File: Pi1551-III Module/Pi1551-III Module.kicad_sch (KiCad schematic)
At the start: 21 parts, among them J1 DC IN, J2 C64_IEC, J3 C64_IEC, J8 Module_Panel, M1 Mounting, M2 Mounting, M3 Mounting, M4 Mounting, U1 7406

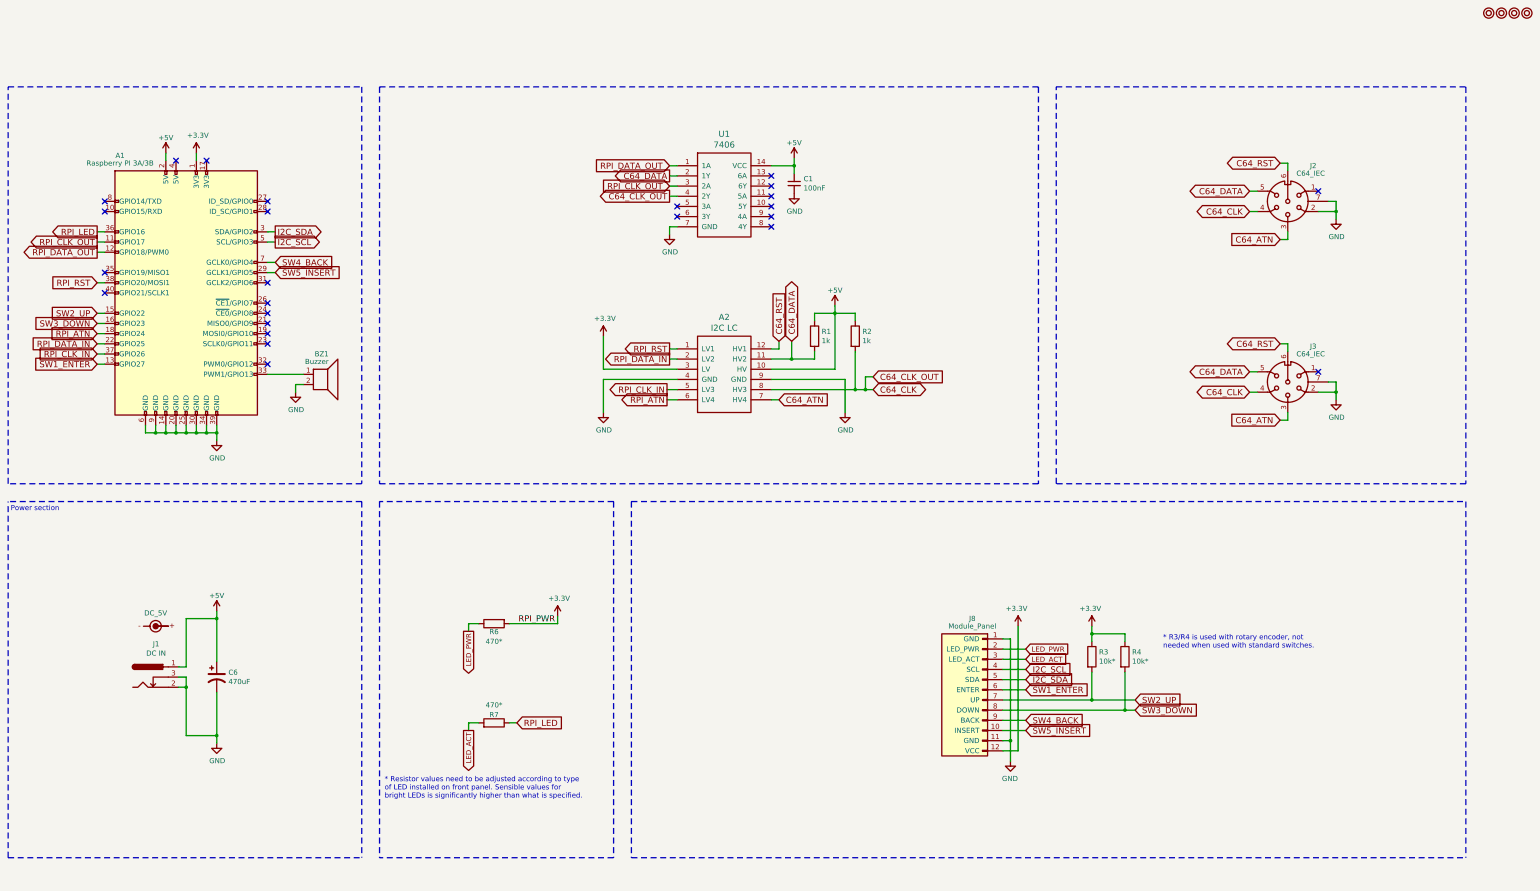
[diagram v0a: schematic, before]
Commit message: PI1551 branding and Microgramma font labels
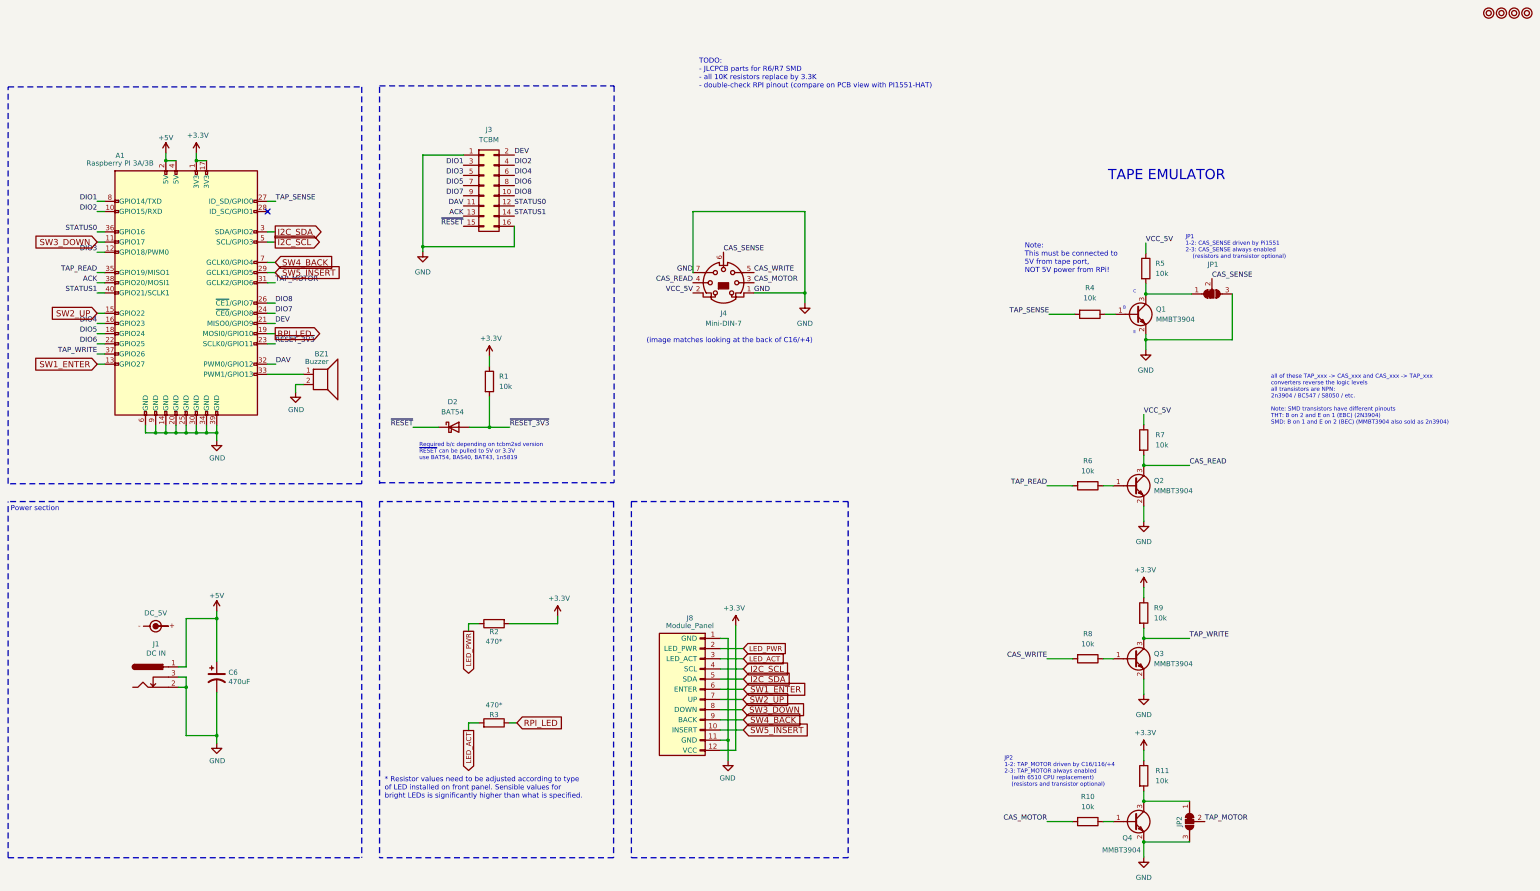
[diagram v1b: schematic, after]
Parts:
- removed A2: I2C LC, IIC_4CH_Level_Converter:4CH_I2C_Level_Converter, symbol 4ch_i2c_level_converter:4CH_I2C_Level_Converter
- removed C1: 100nF, Capacitor_THT:C_Disc_D4.7mm_W2.5mm_P5.00mm, symbol Device:C_Small
- removed J2, J3: C64_IEC, C64_IEC:DIN6_IEC, symbol C64_IEC:C64_IEC
- removed R2: 1k, resistor:R_Axial_DIN0207_L6.3mm_D2.5mm_P10.16mm_Horizontal, symbol Device:R
- removed R3: 10k*, resistor:R_Axial_DIN0207_L6.3mm_D2.5mm_P10.16mm_Horizontal, symbol Device:R
- removed U1: 7406, Package_DIP:DIP-14_W7.62mm_Socket_LongPads, symbol 7406:7406
- added D2: BAT54, Diode_SMD:D_SOD-123, symbol Device:D_Schottky
- added J3: TCBM, Connector_IDC:IDC-Header_2x08_P2.54mm_Vertical, symbol Connector_Generic:Conn_02x08_Odd_Even
- added J4: Mini-DIN-7, Conn_DIN_round:Mini_DIN_round_7_canned, symbol Connector:Mini-DIN-7
- added JP1, JP2: SolderJumper_3_Bridged12, Jumper:SolderJumper-3_P1.3mm_Bridged12_RoundedPad1.0x1.5mm_NumberLabels, symbol Jumper:SolderJumper_3_Bridged12
- added Q1, Q2, Q3, Q4: MMBT3904, Package_TO_SOT_SMD:SOT-23_Handsoldering, symbol Transistor_BJT:MMBT3904
- added R10, R11, R5, R6, R7, R8, R9: 10k, Resistor_SMD:R_0805_2012Metric_Pad1.20x1.40mm_HandSolder, symbol Device:R
- A1, BZ1, C6, J1, J8, SYM1: now left out of the parts list
- R1: value 1k -> 10k; footprint resistor:R_Axial_DIN0207_L6.3mm_D2.5mm_P10.16mm_Horizontal -> Resistor_SMD:R_0805_2012Metric_Pad1.20x1.40mm_HandSolder; JLCPCB Part # (none) -> C22356686; JLCPCB URL (none) -> https://jlcpcb.com/partdetail/23790130-RCA0510KFLF/C22356686; MFR.Part # (none) -> RCA0510KFLF
- R2: renamed from R6; footprint resistor:R_Axial_DIN0207_L6.3mm_D2.5mm_P10.16mm_Horizontal -> Resistor_SMD:R_0805_2012Metric_Pad1.20x1.40mm_HandSolder
- R3: renamed from R7; footprint resistor:R_Axial_DIN0207_L6.3mm_D2.5mm_P10.16mm_Horizontal -> Resistor_SMD:R_0805_2012Metric_Pad1.20x1.40mm_HandSolder
- R4: value 10k* -> 10k; footprint resistor:R_Axial_DIN0207_L6.3mm_D2.5mm_P10.16mm_Horizontal -> Resistor_SMD:R_0805_2012Metric_Pad1.20x1.40mm_HandSolder; JLCPCB Part # (none) -> C22356686; JLCPCB URL (none) -> https://jlcpcb.com/partdetail/23790130-RCA0510KFLF/C22356686; MFR.Part # (none) -> RCA0510KFLF
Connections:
- net C64_DATA is gone; now on net ~{RESET_3V3}: R1.2
- net RPI_CLK_OUT is gone; now on net SW3_DOWN: A1.11 (GPIO17)
- net +3.3V: now also A1.17 (3V3), R1.1, R11.1, R9.1; no longer R4.1
- net +5V: now also A1.4 (5V); no longer R1.1
- net GND: now also J3.1 (Pin_1), J3.16 (Pin_16), J4.1, J4.7, JP1.3 (B), JP2.3 (B), Q1.2 (E), Q2.2 (E), Q3.2 (E), Q4.2 (E)
- net RPI_LED: now also A1.19 (MOSI0/GPIO10); no longer A1.36 (GPIO16)
- net SW3_DOWN: no longer A1.16 (GPIO23), R4.2
- net DIO2: now reaches A1.10 (GPIO15/RXD)
- net DIO2: now also J3.4 (Pin_4)
- net DEV: now reaches A1.21 (MISO0/GPIO9)
- net DEV: now also J3.2 (Pin_2)
- net ~{RESET_3V3}: now reaches A1.23 (SCLK0/GPIO11)
- net ~{RESET_3V3}: now also D2.2 (A)
- net DIO7: now reaches A1.24 (~{CE0}/GPIO8)
- net DIO7: now also J3.9 (Pin_9)
- net DIO8: now reaches A1.26 (~{CE1}/GPIO7)
- net DIO8: now also J3.10 (Pin_10)
- net TAP_SENSE: now reaches A1.27 (ID_SD/GPIO0)
- net TAP_SENSE: now also R4.2
- net TAP_MOTOR: now reaches A1.31 (GCLK2/GPIO6)
- net TAP_MOTOR: now also JP2.2 (C)
- net DAV: now reaches A1.32 (PWM0/GPIO12)
- net DAV: now also J3.11 (Pin_11)
- net TAP_READ: now reaches A1.35 (GPIO19/MISO1)
- net TAP_READ: now also R6.2
- net STATUS1: now reaches A1.40 (GPIO21/SCLK1)
- net STATUS1: now also J3.14 (Pin_14)
- net DIO1: now reaches A1.8 (GPIO14/TXD)
- net DIO1: now also J3.3 (Pin_3)
- net RPI_ATN renamed DIO5
- net DIO5: now also J3.7 (Pin_7)
- net RPI_CLK_IN renamed TAP_WRITE
- net TAP_WRITE: now also Q3.3 (C), R9.2
- net RPI_DATA_IN renamed DIO6
- net DIO6: now also J3.8 (Pin_8)
- net RPI_DATA_OUT renamed DIO3
- net DIO3: now also J3.5 (Pin_5)
- net RPI_RST renamed ACK
- net ACK: now also J3.13 (Pin_13)
- new net: Q2.1 (B), R6.1
- new net: JP1.1 (A), Q1.3 (C), R5.2
- new net: JP2.1 (A), Q4.3 (C), R11.2
- new net: Q1.1 (B), R4.1
- new net: Q3.1 (B), R8.1
- new net: Q4.1 (B), R10.1
- new net CAS_MOTOR: J4.3, R10.2
- new net CAS_READ: J4.4, Q2.3 (C), R7.2
- new net CAS_SENSE: J4.6, JP1.2 (C)
- new net CAS_WRITE: J4.5, R8.2
- new net DIO4: A1.16 (GPIO23), J3.6 (Pin_6)
- new net STATUS0: A1.36 (GPIO16), J3.12 (Pin_12)
- new net VCC_5V: J4.2, R5.1, R7.1
- new net ~{RESET}: D2.1 (K), J3.15 (Pin_15)
- no-connect marks 25 -> 1
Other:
- note added: "(image matches looking at the back of C16/+4)"
- note added: "B"
- note added: "C"
- note added: "E"
- note added: "JP1 1-2: CAS_SENSE driven by Pi1551 2-3: CAS_SENSE always enabled (resistors and transistor optional)"
- note added: "JP2 1-2: TAP_MOTOR driven by C16/116/+4 2-3: TAP_MOTOR always enabled (with 6510 CPU replacement) (resistors and transistor optional)"
- note added: "Note: This must be connected to 5V from tape port, NOT 5V power from RPi!"
- note added: "Required b/c depending on tcbm2sd version ~{RESET} can be pulled to 5V or 3.3V use BAT54, BAS40, BAT43, 1n5819"
- note added: "TAPE EMULATOR"
- note added: "TODO: - JLCPCB parts for R6/R7 SMD - all 10K resistors replace by 3.3K - double-check RPI pinout (compare on PCB view with PI1551-HAT)"
- note added: "all of these TAP_xxx -> CAS_xxx and CAS_xxx -> TAP_xxx converters reverse the logic levels all transistors are NPN: 2n3904 / BC547 / S8050 / etc. Note: SMD transistors have different pinouts THT: B on 2 and E on 1 (EBC) (2N3904) SMD: B on 1 and E on 2 (BEC) (MMBT3904 also sold as 2n3904)"
- note removed: "* R3/R4 is used with rotary encoder, not needed when used with standard switches."
- moved on the sheet: J8

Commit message: all 10K resistors to 3.3K, JLPCB part numbers for 470R resistors, 1.2mm track width for 5V - as short as possible
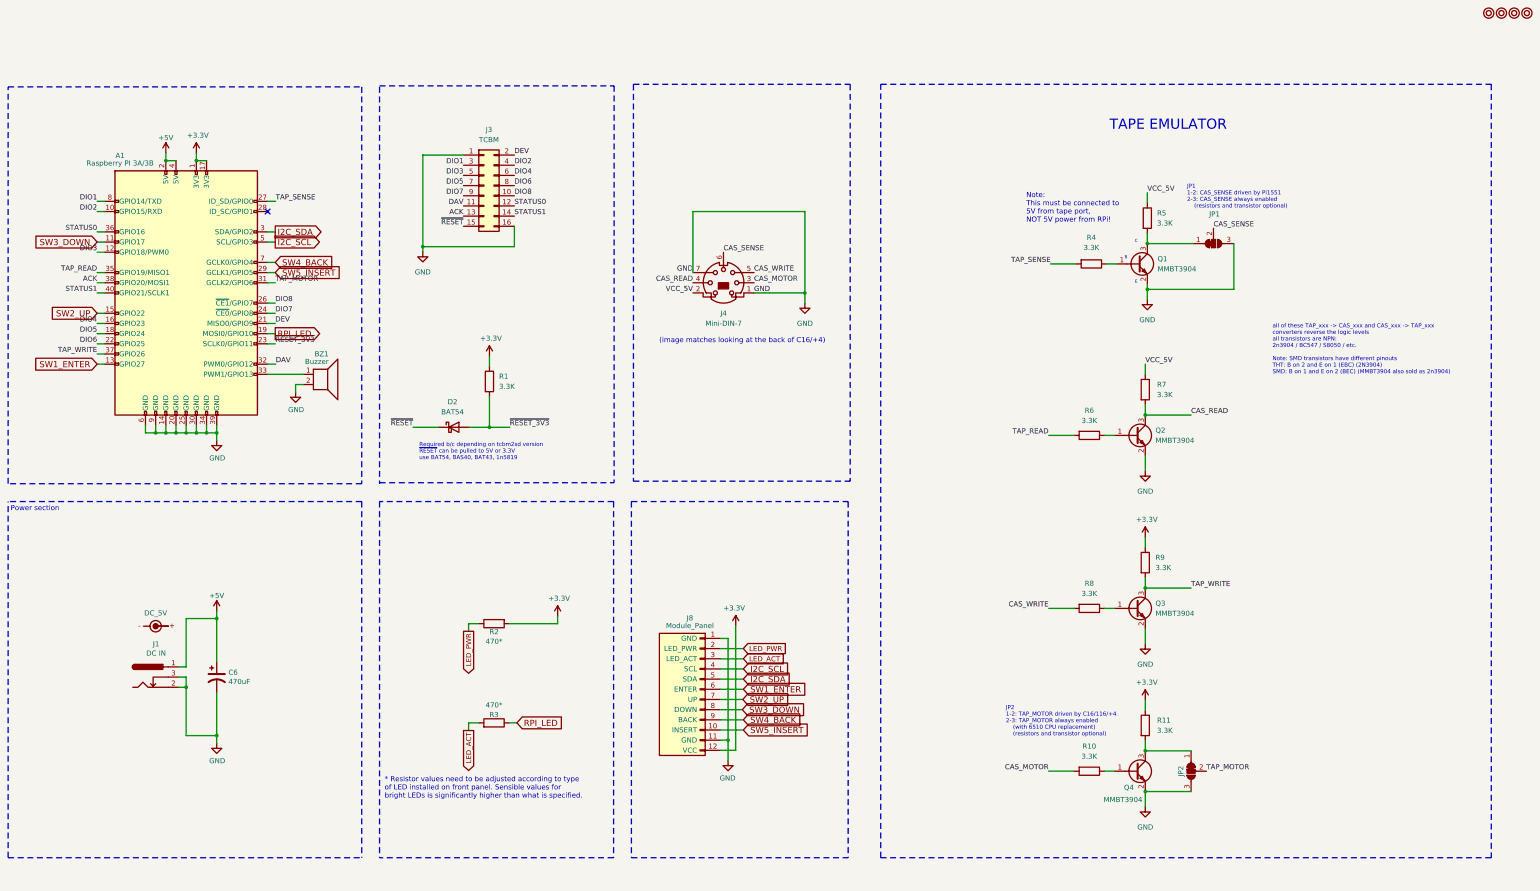
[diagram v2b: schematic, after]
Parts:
- R1, R10, R11, R4, R5, R6, R7, R8, R9: value 10k -> 3.3K; JLCPCB Part # C22356686 -> C26010; JLCPCB URL https://jlcpcb.com/partdetail/23790130-RCA0510KFLF/C22356686 -> https://jlcpcb.com/partdetail/26753-0805W8F3301T5E/C26010; MFR.Part # RCA0510KFLF -> 0805W8F3301T5E
- R2, R3: JLCPCB Part # (none) -> C17710; JLCPCB URL (none) -> https://jlcpcb.com/partdetail/18398-0805W8F4700T5E/C17710; MFR.Part # (none) -> 0805W8F4700T5E
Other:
- note removed: "TODO: - JLCPCB parts for R6/R7 SMD - all 10K resistors replace by 3.3K - double-check RPI pinout (compare on PCB view with PI1551-HAT)"
- moved on the sheet: JP1, JP2, Q1, Q2, Q3, Q4, R10, R11, R4, R5, R6, R7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
